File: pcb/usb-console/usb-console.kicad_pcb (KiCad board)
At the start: 2 copper layers, 18 x 36 mm, 12 parts, among them J1 USB_B_Mini, J2 Conn_02x02_Odd_Even, U1 CH340E

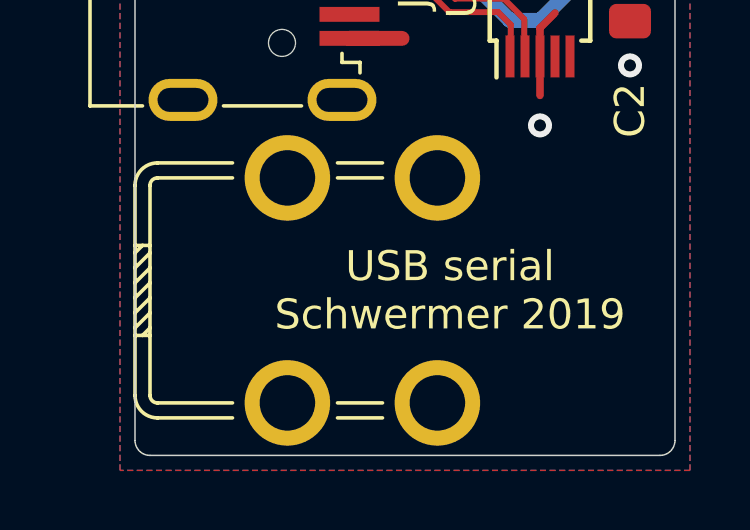
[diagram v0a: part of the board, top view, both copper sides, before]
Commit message: PCBs sent to fab
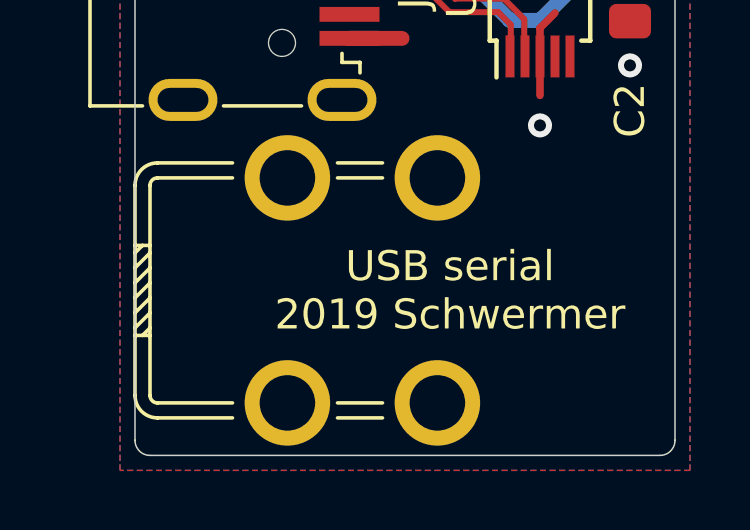
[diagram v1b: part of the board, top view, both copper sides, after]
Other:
- board text added: "USB serial 2019 Schwermer"
- board text removed: "USB serial Schwermer 2019"
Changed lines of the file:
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@@
   (gr_arc (start 127.5 90) (end 128 90) (angle -90) (layer Edge.Cuts) (width 0.05))
   (gr_arc (start 110.5 90) (end 110.5 89.5) (angle -90) (layer Edge.Cuts) (width 0.05))
-  (gr_text "USB serial\nSchwermer 2019" (at 120.5 120) (layer F.SilkS)
+  (gr_text "USB serial\n2019 Schwermer" (at 120.5 120) (layer F.SilkS)
     (effects (font (size 1 1) (thickness 0.15)))
   )
